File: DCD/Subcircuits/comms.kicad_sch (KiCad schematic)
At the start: 11 parts, among them J1 UMPS-04-03.5-G-VT-SM-WT, J2 UMPS-04-03.5-G-VT-SM-WT, J3 UMPS-04-03.5-G-VT-SM-WT, J4 UMPS-04-03.5-G-VT-SM-WT, J5 Conn_02x04_Top_Bottom

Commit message: Added the footprint
My libraries are fucked for some reason so I have to change machines to
pull footprints and add components
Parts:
- J5: footprint Connector_PinHeader_2.54mm:PinHeader_2x04_P2.54mm_Vertical_SMD -> Connector_PinHeader_2.54mm:PinHeader_2x04_P2.54mm_Vertical
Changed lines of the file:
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@@
 			)
 		)
-		(property "Footprint" "Connector_PinHeader_2.54mm:PinHeader_2x04_P2.54mm_Vertical_SMD"
+		(property "Footprint" "Connector_PinHeader_2.54mm:PinHeader_2x04_P2.54mm_Vertical"
 			(at 34.29 82.55 0)
 			(effects

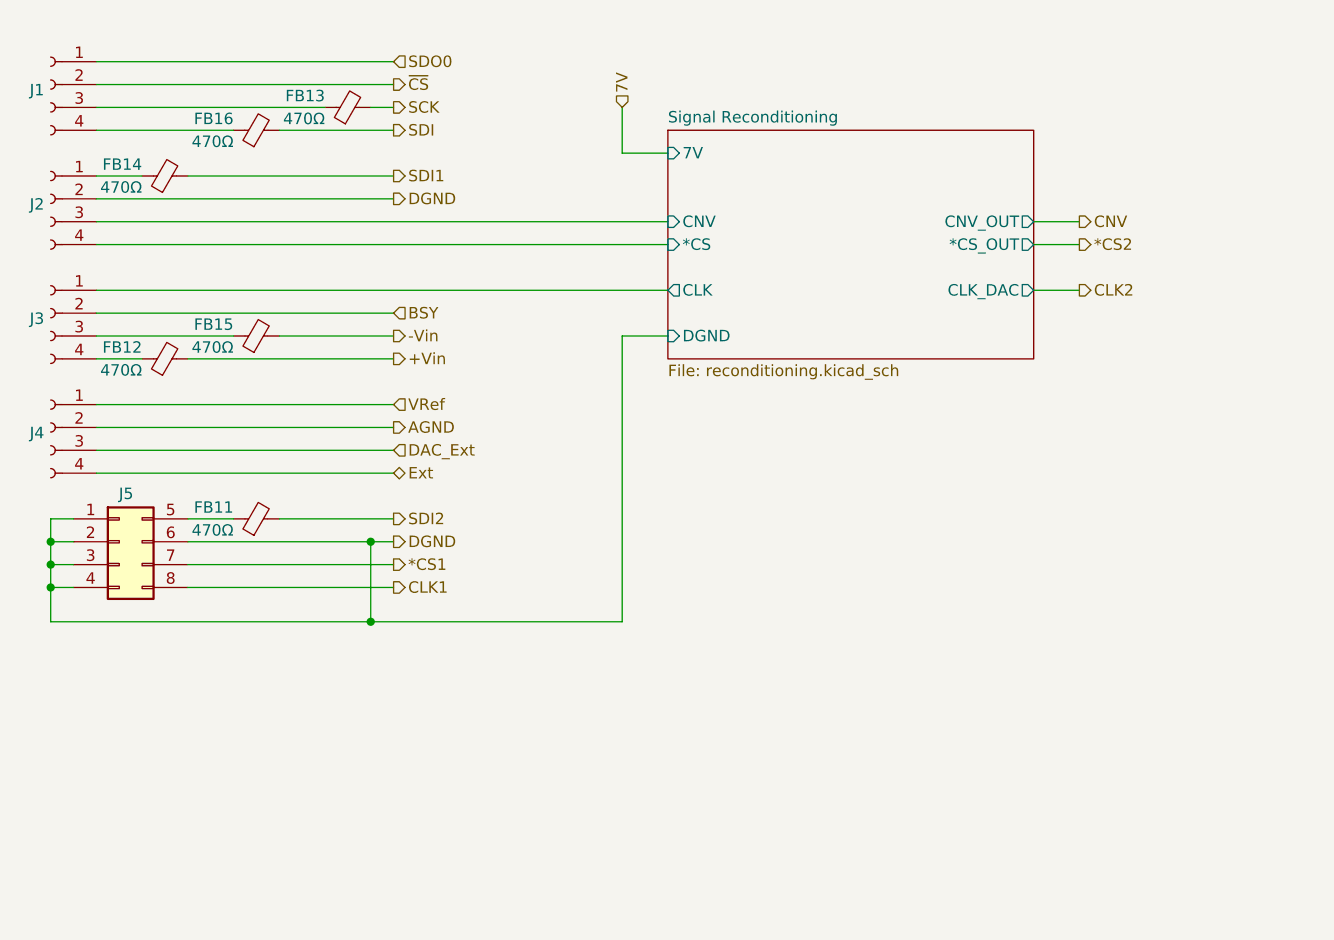
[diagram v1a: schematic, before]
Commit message: Almost finished the layout. Did all of the power and top layer
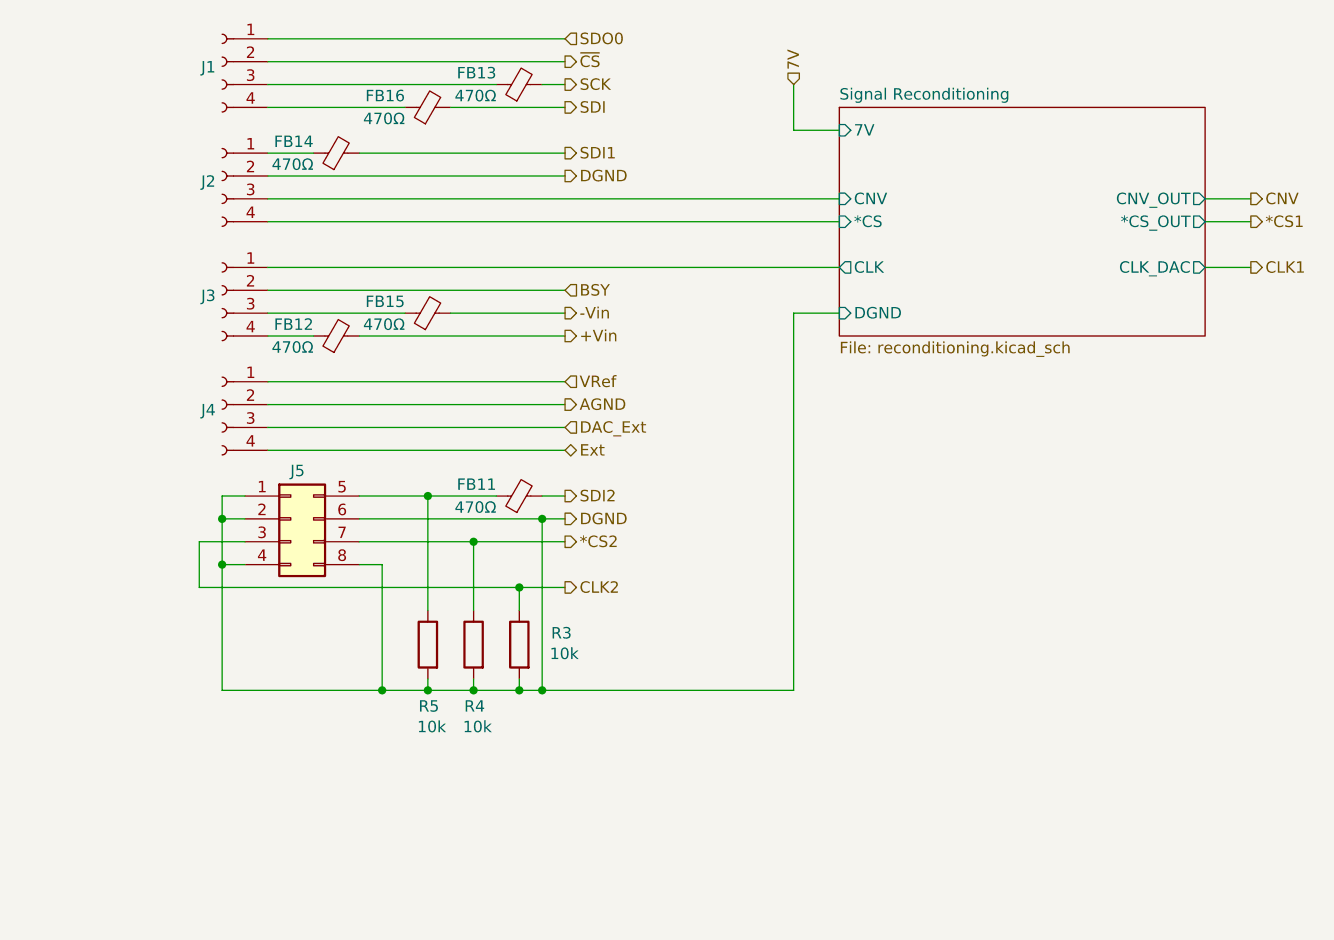
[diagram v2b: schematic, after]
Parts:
- added R3, R4, R5: 10k, Resistor_SMD:R_0603_1608Metric, symbol Device:R
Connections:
- net *CS1: no longer J5.7 (Pin_7)
- net *CS2: now also J5.7 (Pin_7), R4.1
- net CLK1: no longer J5.8 (Pin_8)
- net CLK2: now also J5.3 (Pin_3), R3.1
- net DGND: now also J5.8 (Pin_8), R3.2, R4.2, R5.2; no longer J5.3 (Pin_3)
- net at FB11.1, J5.5 (Pin_5): now also R5.1
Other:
- moved on the sheet: FB11, FB12, FB13, FB14, FB15, FB16, J1, J2, J3, J4, J5

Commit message: Finished the layout
Modified ground planes separation, finished stiching, fixed drc errors
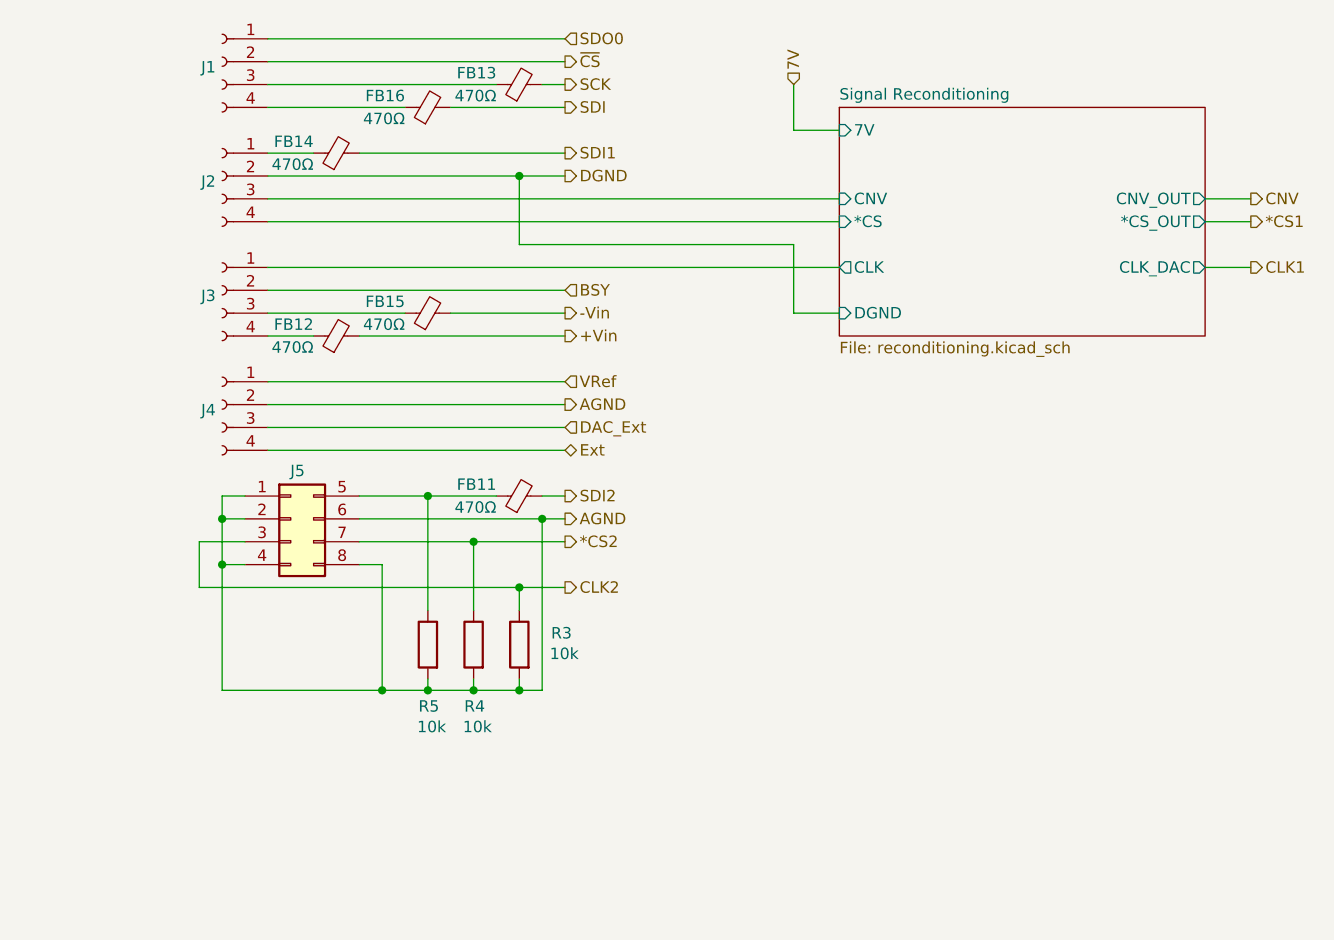
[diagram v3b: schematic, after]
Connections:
- net AGND: now also J5.1 (Pin_1), J5.2 (Pin_2), J5.4 (Pin_4), J5.6 (Pin_6), J5.8 (Pin_8), R3.2, R4.2, R5.2
- net DGND: no longer J5.1 (Pin_1), J5.2 (Pin_2), J5.4 (Pin_4), J5.6 (Pin_6), J5.8 (Pin_8), R3.2, R4.2, R5.2
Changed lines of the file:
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@@
-	)
-	(junction
-		(at 81.28 99.06)
-		(diameter 0)
-		(color 0 0 0 0)
 	)
 	(junction
@@
 	)
 	(junction
+		(at 78.74 41.91)
+		(diameter 0)
+		(color 0 0 0 0)
+	)
+	(junction
 		(at 63.5 99.06)
 		(diameter 0)
@@
 	(wire
 		(pts
-			(xy 109.22 99.06) (xy 81.28 99.06)
-		)
-		(stroke
-			(width 0)
-			(type default)
-		)
-	)
-	(wire
-		(pts
 			(xy 63.5 85.09) (xy 63.5 99.06)
 		)
@@
 	(wire
 		(pts
+			(xy 109.22 49.53) (xy 109.22 57.15)
+		)
+		(stroke
+			(width 0)
+			(type default)
+		)
+	)
+	(wire
+		(pts
 			(xy 154.94 52.07) (xy 160.02 52.07)
 		)
@@
 	(wire
 		(pts
+			(xy 78.74 41.91) (xy 83.82 41.91)
+		)
+		(stroke
+			(width 0)
+			(type default)
+		)
+	)
+	(wire
+		(pts
 			(xy 45.72 80.01) (xy 45.72 85.09)
 		)
@@
 	(wire
 		(pts
-			(xy 50.8 41.91) (xy 83.82 41.91)
+			(xy 50.8 41.91) (xy 78.74 41.91)
 		)
 		(stroke
@@
 	(wire
 		(pts
+			(xy 78.74 49.53) (xy 109.22 49.53)
+		)
+		(stroke
+			(width 0)
+			(type default)
+		)
+	)
+	(wire
+		(pts
 			(xy 50.8 72.39) (xy 83.82 72.39)
 		)
@@
 	(wire
 		(pts
+			(xy 78.74 41.91) (xy 78.74 49.53)
+		)
+		(stroke
+			(width 0)
+			(type default)
+		)
+	)
+	(wire
+		(pts
 			(xy 45.72 80.01) (xy 48.26 80.01)
 		)
@@
 		(pts
 			(xy 45.72 85.09) (xy 48.26 85.09)
-		)
-		(stroke
-			(width 0)
-			(type default)
-		)
-	)
-	(wire
-		(pts
-			(xy 109.22 57.15) (xy 109.22 99.06)
 		)
 		(stroke
@@
 		)
 	)
+	(hierarchical_label "AGND"
+		(shape output)
+		(at 83.82 80.01 0)
+		(effects
+			(font
+				(size 1.27 1.27)
+			)
+			(justify left)
+		)
+	)
 	(hierarchical_label "SDI1"
 		(shape output)
@@
 		(effects
 			(font
-				(size 1.27 1.27)
-			)
-			(justify left)
-		)
-	)
-	(hierarchical_label "DGND"
-		(shape output)
-		(at 83.82 80.01 0)
-		(effects
-			(font

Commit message: Added components part numbers and stuff. Added termination resistors
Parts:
- J5: Link (none) -> https://www.mouser.com/ProductDetail/Molex/90131-0763?qs=KO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; Order number (none) -> 538-90131-0763; Part number (none) -> 90131-0763; Supplier (none) -> Mouser
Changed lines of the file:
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@@
+			)
+		)
+		(property "Link" "https://www.mouser.com/ProductDetail/Molex/90131-0763?qs=KObwnG1V4zuKPiIchrbqlw%3D%3D"
+			(at 53.34 80.01 0)
+			(effects
+				(font
+					(size 1.27 1.27)
+				)
+				(hide yes)
+			)
+		)
+		(property "Supplier" "Mouser"
+			(at 53.34 80.01 0)
+			(effects
+				(font
+					(size 1.27 1.27)
+				)
+				(hide yes)
+			)
+		)
+		(property "Part number" " 90131-0763 "
+			(at 53.34 80.01 0)
+			(effects
+				(font
+					(size 1.27 1.27)
+				)
+				(hide yes)
+			)
+		)
+		(property "Order number" "538-90131-0763 "
+			(at 53.34 80.01 0)
+			(effects
+				(font
+					(size 1.27 1.27)
+				)
+				(hide yes)
 			)
 		)

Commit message: Bodges
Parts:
- removed FB13, FB16: 470Ω, Inductor_SMD:L_0603_1608Metric, symbol Device:FerriteBead_Small
- added R28, R29, R30, R31, R32, R33: 10k, Resistor_SMD:R_0603_1608Metric, symbol Device:R
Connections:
- net DGND: now also R31.2, R32.2, R33.2
- net SCK: now also R29.2, R32.1
- net SDI: now also R28.2, R33.1
- net ~{CS}: now also R30.2, R31.1; no longer J1.2 (Pin_2)
- net at J1.3 (Pin_3): now also R29.1
- net at J1.4 (Pin_4): now also R28.1
- new net: J1.2 (Pin_2), R30.1
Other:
- moved on the sheet: FB11, FB12, FB14, FB15, J1, J2, J3, J4, J5, R3, R4, R5
